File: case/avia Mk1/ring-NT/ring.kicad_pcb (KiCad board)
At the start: 2 copper layers, 44 x 43.6 mm, 1 part

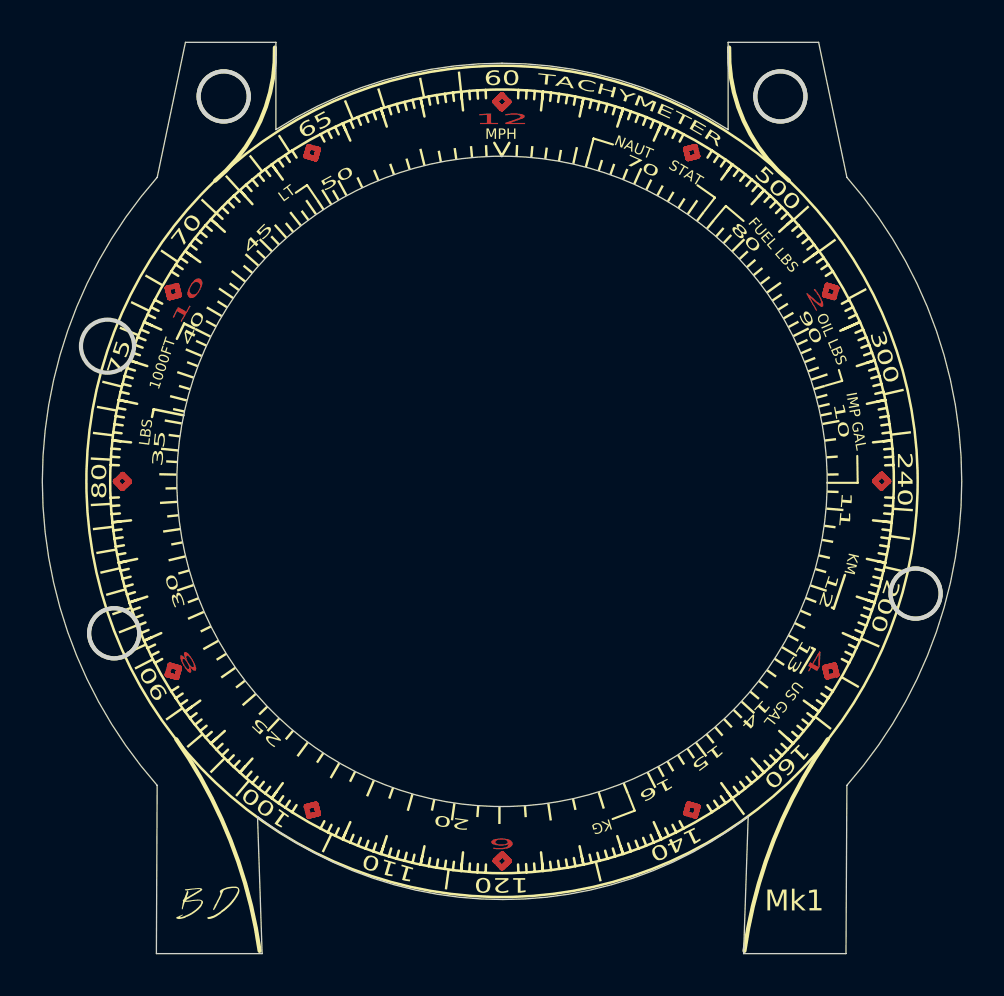
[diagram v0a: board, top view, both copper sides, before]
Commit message: no multiple definitions error
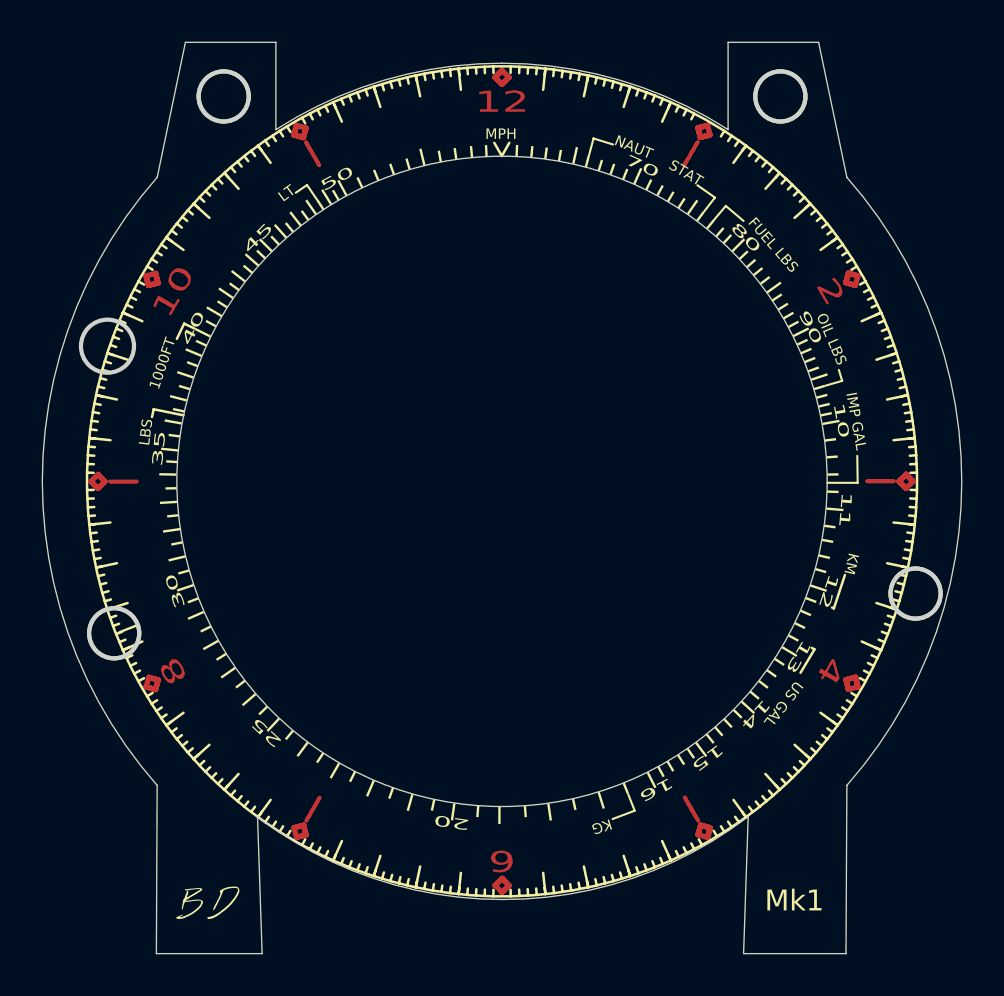
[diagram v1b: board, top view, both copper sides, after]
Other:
- board text removed: "100"
- board text removed: "110"
- board text removed: "120"
- board text removed: "140"
- board text removed: "160"
- board text removed: "200"
- board text removed: "240"
- board text removed: "300"
- board text removed: "500"
- board text removed: "60"
- board text removed: "65"
- board text removed: "75"
- board text removed: "A"
- board text removed: "C"
- board text removed: "E"
- board text removed: "H"
- board text removed: "M"
- board text removed: "R"
- board text removed: "T"
- board text removed: "Y"
